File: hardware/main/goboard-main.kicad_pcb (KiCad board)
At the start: 2 copper layers, 304.7 x 135.9 mm, 152 parts, among them J1 USB_C_Receptacle_USB2.0, J2 Conn_02x05_Top_Bottom, J3 Conn_01x01, SW1 Esc, SW10 a, SW12 Fn, SW13 F2, SW14 2, SW15 w, SW16 s, SW17 z, SW18 Tux, SW19 F3, SW2 F1, SW20 3, SW21 e, SW22 d, SW23 c, SW24 Alt, SW25 F4, SW26 4, SW27 r, SW28 f, SW29 v, SW3 tilde, SW30 SW_SP3T, SW31 F5, SW32 5, SW33 t, SW34 g, SW35 b, SW36 F6, SW37 6, SW38 y, SW39 h, SW4 Tab, SW40 n, SW41 F7, SW42 7, SW43 u, SW44 j, SW45 m, SW46 Space, SW47 F8, SW48 8, SW49 i, SW5 Caps Lock, SW50 k, SW51 ,, SW52 F9, SW53 9, SW54 o, SW55 l, SW56 ., SW57 F10, SW58 0, SW59 p, SW6 Shift, SW60 ;, SW61 /, SW62 Alt Gr, SW63 F11, SW64 -, SW65 [, SW66 ', SW68 F12, SW69 =, SW7 Ctrl, SW70 ], SW71 \, SW72 Shift, SW73 Ctrl, SW74 Print, SW75 Backspace, SW76 Enter, SW77 Left, SW78 Scroll Lock, SW79 Up, SW8 1, SW80 Down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

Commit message: Change value field for the backslash-key
The value "\" caused the FreeCAD-StepUp load to fail due to a parsing
error.
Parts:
- SW71: value \ -> backslash
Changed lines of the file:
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@@
       (effects (font (size 1 1) (thickness 0.15)))
     )
-    (fp_text value "\\" (at -2.54 12.954) (layer "F.Fab")
+    (fp_text value "backslash" (at -2.54 12.954) (layer "F.Fab")
       (effects (font (size 1 1) (thickness 0.15)))
     )

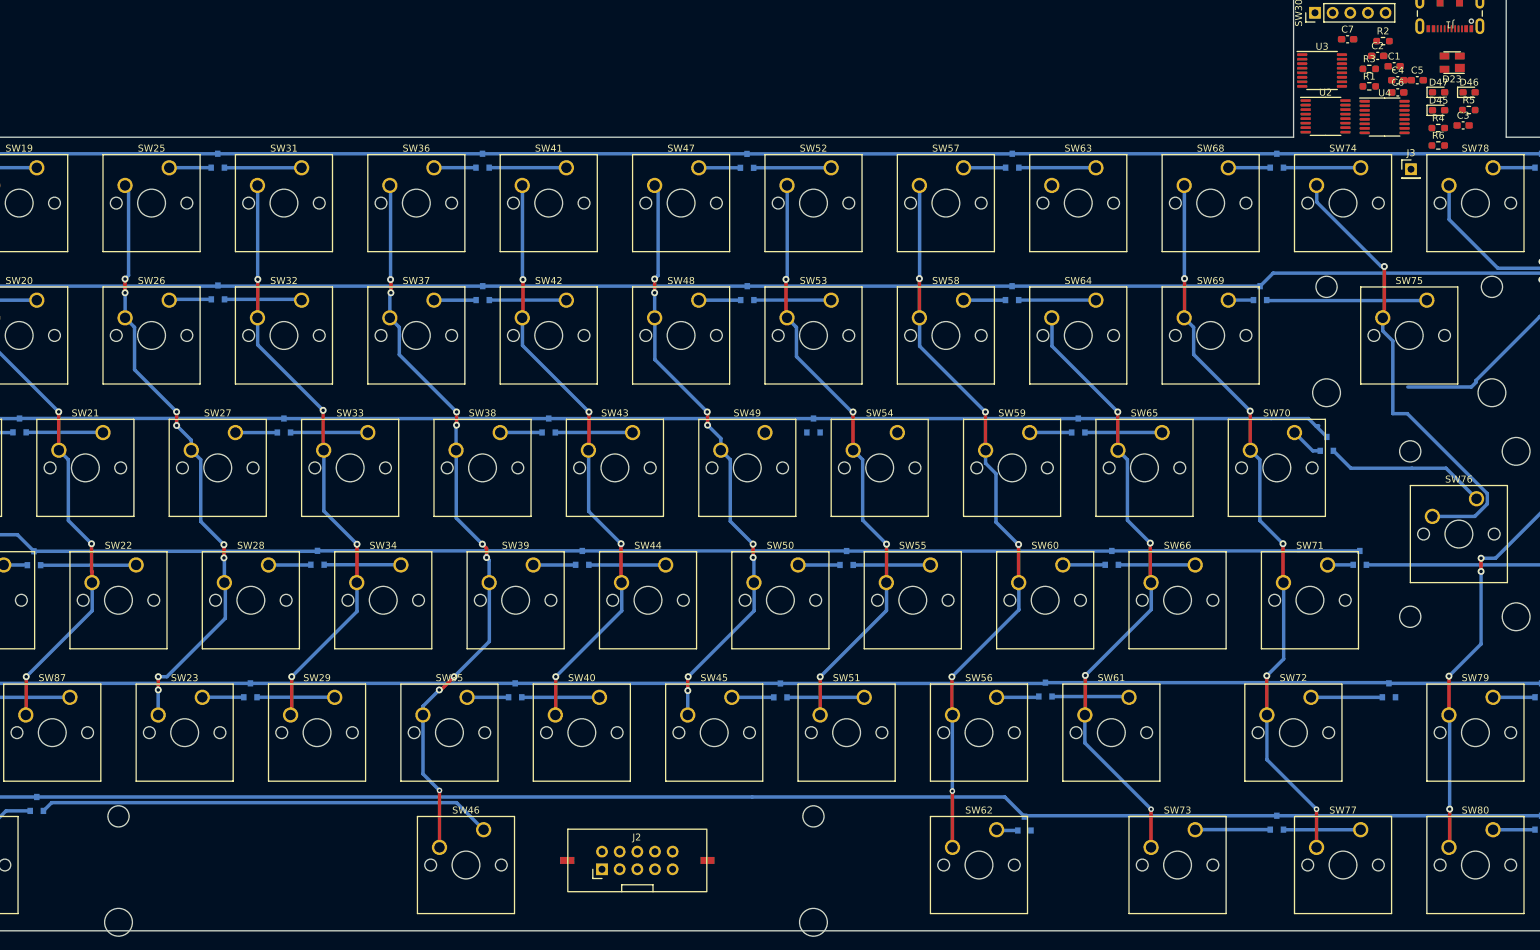
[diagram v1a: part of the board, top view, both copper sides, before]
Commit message: Write out the symbol names for the keys
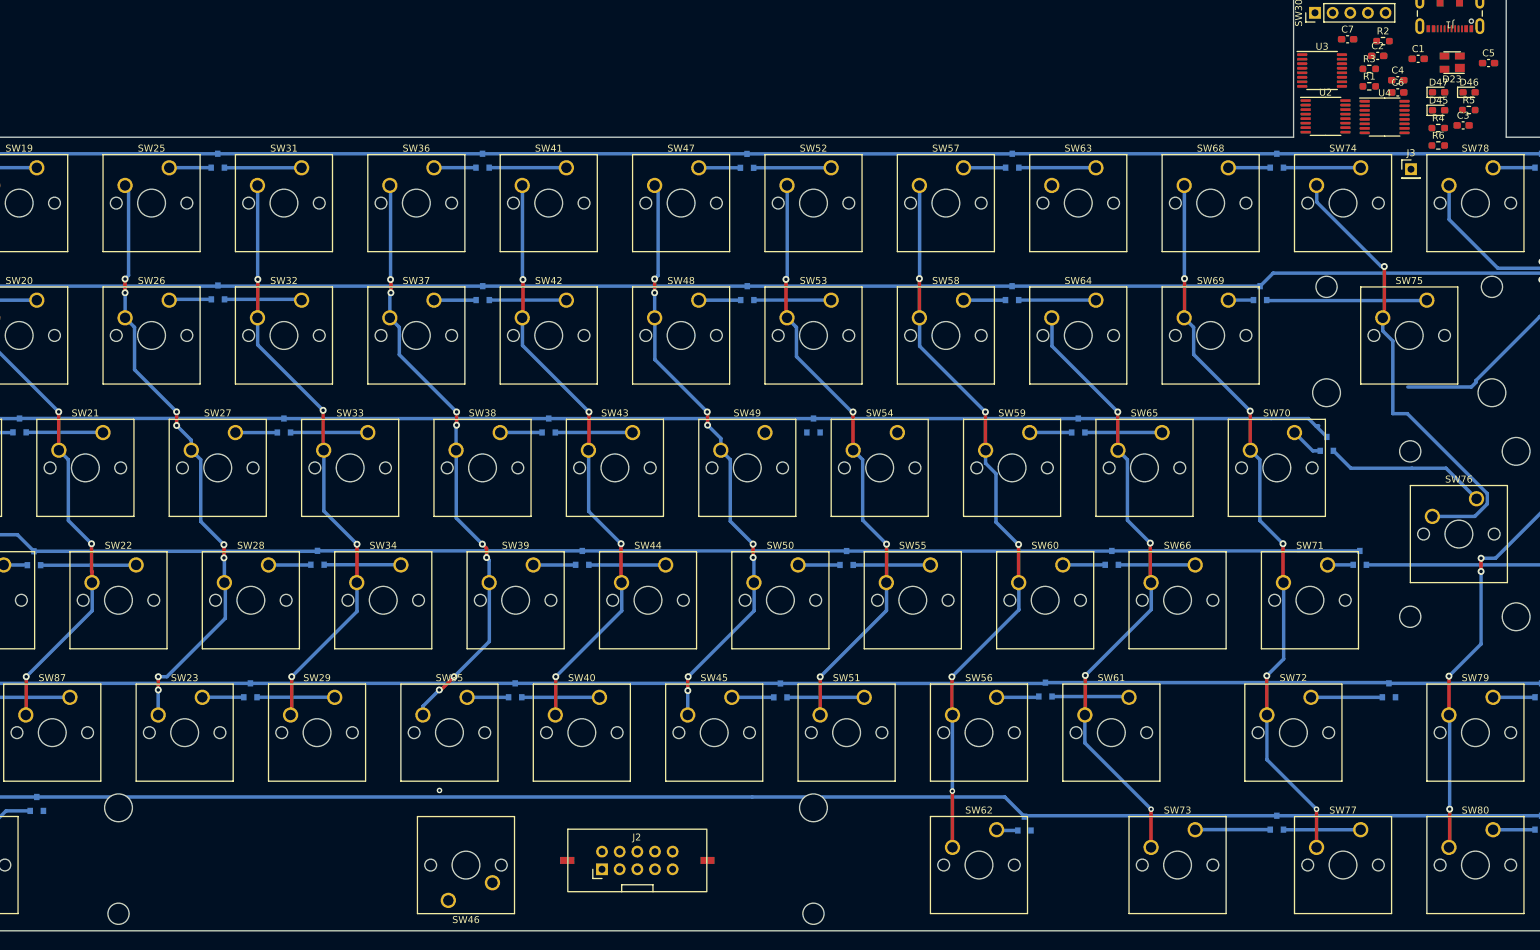
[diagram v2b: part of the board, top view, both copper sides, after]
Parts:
- SW51: value , -> comma
- SW56: value . -> dot
- SW60: value ; -> semicolon
- SW61: value / -> slash
- SW64: value - -> minus
- SW65: value [ -> sq br open
- SW66: value ' -> apostrophe
- SW69: value = -> equal
- SW70: value ] -> sq br close
- moved SW46 11.4 mm to (166.4, 181.6), turned to 180 degrees
- moved C5 10.6 mm to (316.1, 61.1)
- moved C1 3.62 mm to (305.9, 60.5)
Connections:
- net Net-(D39-Pad1) renamed no_connect_(D39-Pad1)
- net Net-(SW30-Pad1) renamed no_connect_(SW30-Pad1)
- net Net-(SW30-Pad2) renamed no_connect_(SW30-Pad2)
- net Net-(SW30-Pad3) renamed no_connect_(SW30-Pad3)
- net Net-(SW30-Pad4) renamed no_connect_(SW30-Pad4)
- net no_connect_150 renamed no_connect_(D40-Pad1)
- net no_connect_151 renamed no_connect_(J1-PadA8)
- net no_connect_152 renamed no_connect_(J1-PadB8)
- net no_connect_153 renamed no_connect_(J2-Pad10)
- net no_connect_154 renamed no_connect_(J2-Pad3)
- net no_connect_155 renamed no_connect_(J2-Pad5)
- net no_connect_156 renamed no_connect_(U1-Pad10)
- net no_connect_157 renamed no_connect_(U1-Pad11)
- net no_connect_158 renamed no_connect_(U1-Pad18)
- net no_connect_159 renamed no_connect_(U1-Pad19)
- net no_connect_160 renamed no_connect_(U1-Pad2)
- net no_connect_161 renamed no_connect_(U1-Pad26)
- net no_connect_162 renamed no_connect_(U1-Pad3)
- net no_connect_163 renamed no_connect_(U1-Pad33)
- net no_connect_164 renamed no_connect_(U1-Pad34)
- net no_connect_165 renamed no_connect_(U1-Pad35)
- net no_connect_166 renamed no_connect_(U1-Pad36)
- net no_connect_167 renamed no_connect_(U1-Pad38)
- net no_connect_168 renamed no_connect_(U1-Pad39)
- net no_connect_169 renamed no_connect_(U1-Pad4)
- net no_connect_170 renamed no_connect_(U1-Pad40)
- net no_connect_171 renamed no_connect_(U1-Pad41)
- net no_connect_172 renamed no_connect_(U1-Pad42)
- net no_connect_173 renamed no_connect_(U1-Pad43)
- net no_connect_174 renamed no_connect_(U1-Pad44)
- net no_connect_175 renamed no_connect_(U1-Pad45)
- net no_connect_176 renamed no_connect_(U1-Pad46)
- net no_connect_177 renamed no_connect_(U1-Pad47)
- net no_connect_178 renamed no_connect_(U1-Pad48)
- net no_connect_179 renamed no_connect_(U1-Pad49)
- net no_connect_180 renamed no_connect_(U1-Pad5)
- net no_connect_181 renamed no_connect_(U1-Pad50)
- net no_connect_182 renamed no_connect_(U1-Pad51)
- net no_connect_183 renamed no_connect_(U1-Pad52)
- net no_connect_184 renamed no_connect_(U1-Pad53)
- net no_connect_185 renamed no_connect_(U1-Pad54)
- net no_connect_186 renamed no_connect_(U1-Pad55)
- net no_connect_187 renamed no_connect_(U1-Pad6)
- net no_connect_188 renamed no_connect_(U1-Pad7)
- net no_connect_189 renamed no_connect_(U1-Pad8)
- net no_connect_190 renamed no_connect_(U1-Pad9)
- net no_connect_191 renamed no_connect_(U2-Pad6)
- net no_connect_192 renamed no_connect_(U2-Pad7)
- net no_connect_193 renamed no_connect_(U2-Pad9)
- net no_connect_194 renamed no_connect_(U3-Pad7)
- net no_connect_195 renamed no_connect_(U4-Pad10)
- net no_connect_196 renamed no_connect_(U4-Pad7)
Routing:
- net Net-(D12-Pad1): track 65.4 -> 0.00 mm
- net Net-(SW35-Pad2): track 106.5 -> 86.5 mm
- net Net-(D40-Pad2): track 10.8 -> 21.9 mm
- net Net-(D34-Pad1): track 11.1 -> 0.00 mm

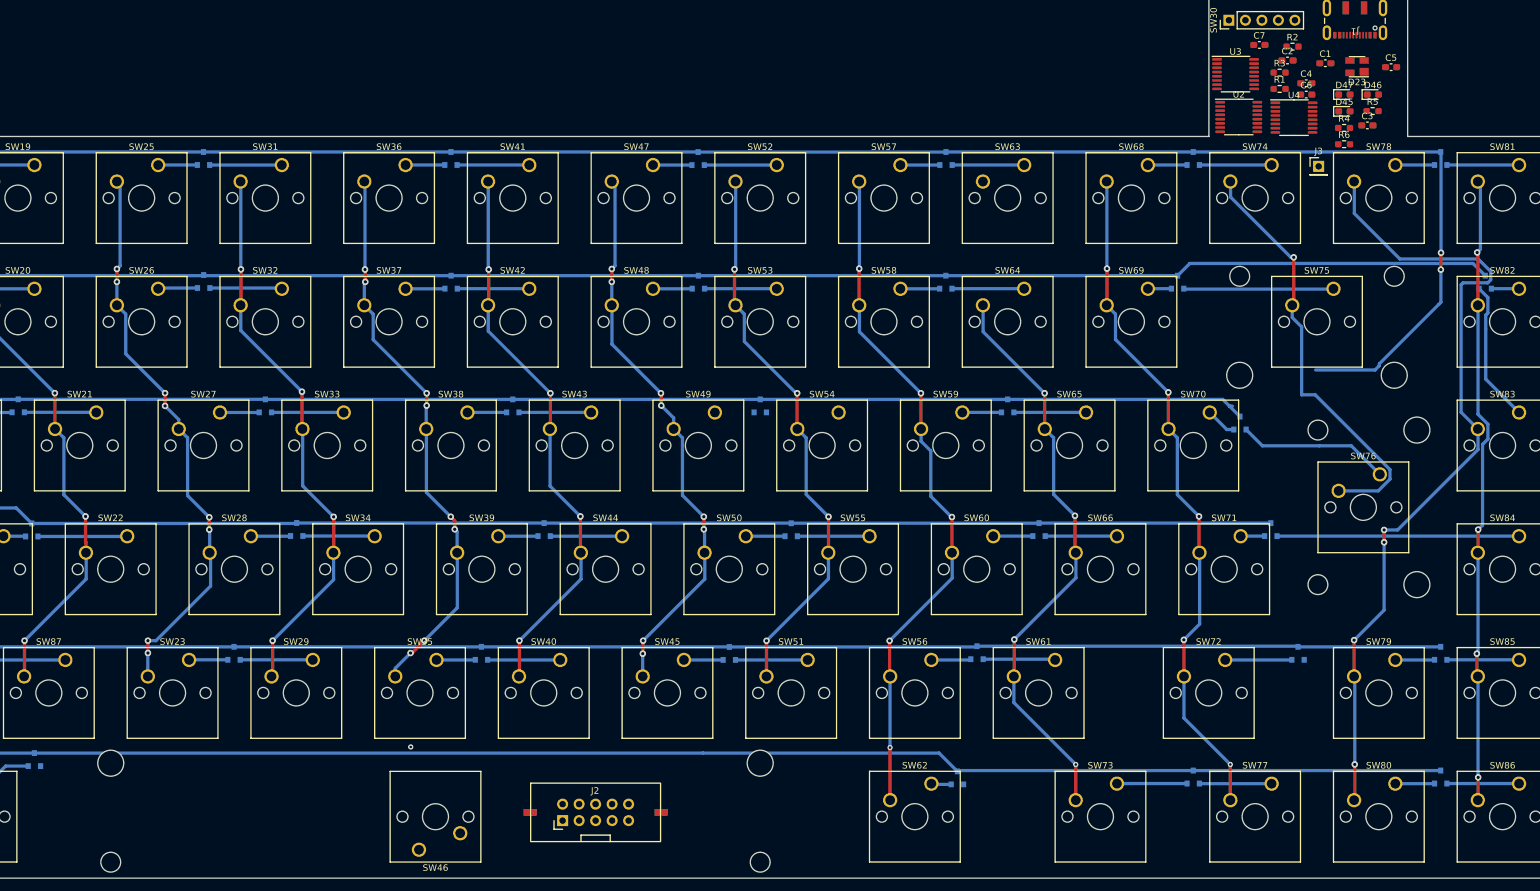
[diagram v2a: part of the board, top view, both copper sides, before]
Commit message: Revert to a key layout with a menu key between alt gr and ctrl
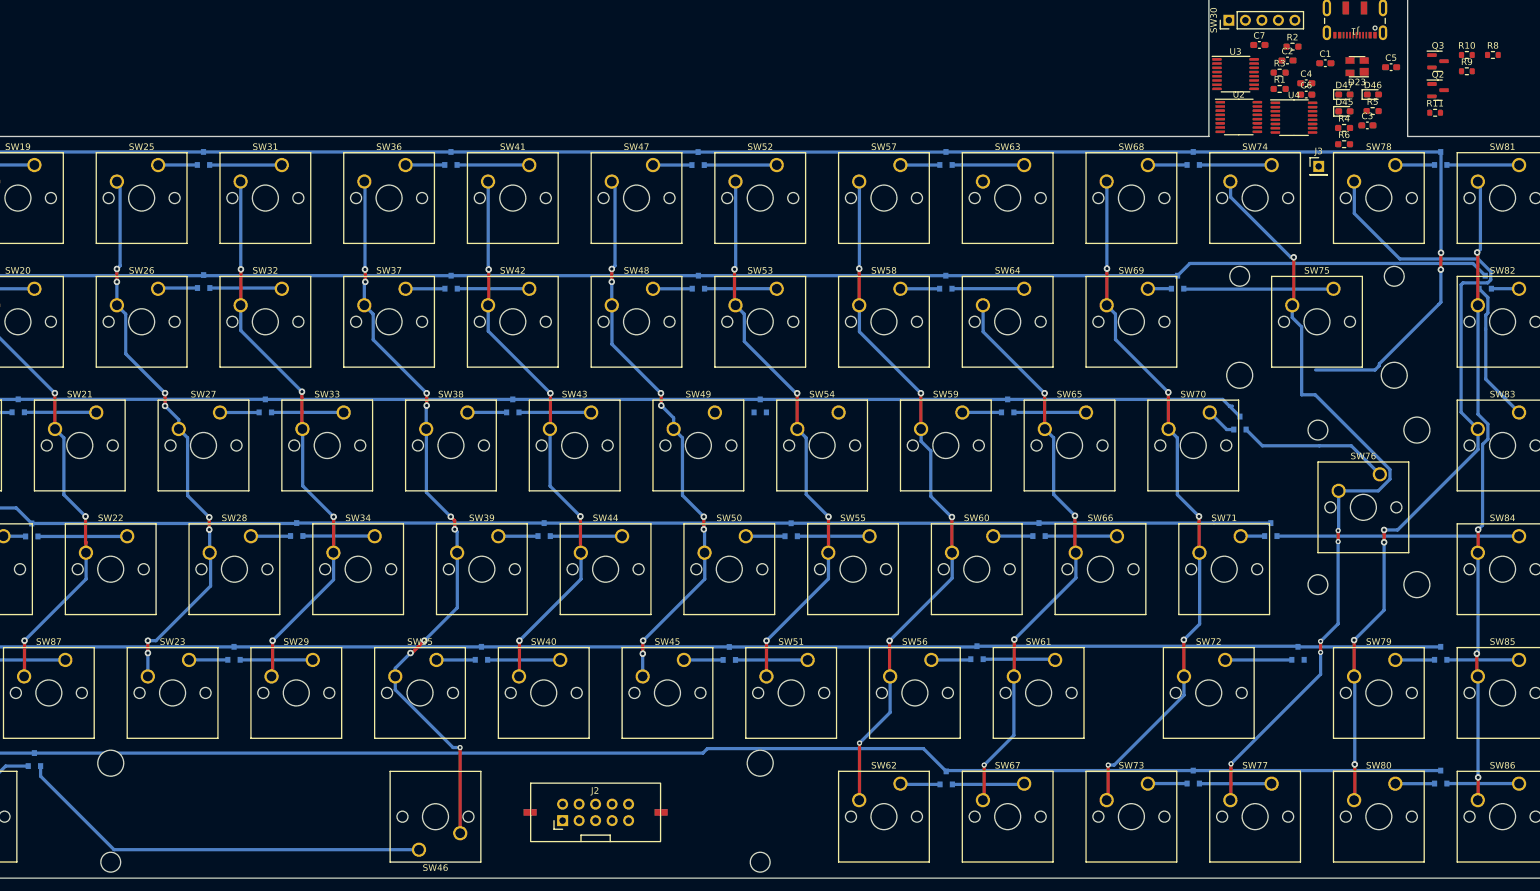
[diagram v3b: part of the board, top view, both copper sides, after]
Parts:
- added Q2: BC807, Package_TO_SOT_SMD:SOT-23, F.Cu at (323.3, 64.7)
- added Q3: BC817, Package_TO_SOT_SMD:SOT-23, F.Cu at (323.3, 60.2)
- added R10: 30, Resistor_SMD:R_0603_1608Metric, F.Cu at (327.7, 59.2)
- added R11: 30, Resistor_SMD:R_0603_1608Metric, F.Cu at (322.8, 68.2)
- added R8: 1K, Resistor_SMD:R_0603_1608Metric, F.Cu at (331.7, 59.2)
- added R9: 1K, Resistor_SMD:R_0603_1608Metric, F.Cu at (327.7, 61.8)
- added SW67: Menu, footprints:SW_Cherry_MX_1.00u_PCB, F.Cu at (259.6, 171.4)
- SW62, SW73: footprint footprints:SW_Cherry_MX_1.50u_PCB -> footprints:SW_Cherry_MX_1.00u_PCB
- moved SW62 4.76 mm to (240.5, 171.4)
- moved SW73 4.76 mm to (278.6, 171.4)
- moved D34 1.72 mm to (247.6, 170.6)
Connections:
- D40 pad 1: no_connect_(D40-Pad1) -> Net-(D40-Pad1)
- SW73 pad 1: Net-(D34-Pad1) -> Net-(D40-Pad2)
- SW73 pad 2: Net-(SW61-Pad2) -> Net-(SW68-Pad2)
- SW77 pad 1: Net-(D40-Pad2) -> Net-(D40-Pad1)
- SW77 pad 2: Net-(SW68-Pad2) -> Net-(SW74-Pad2)
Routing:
- net Net-(D12-Pad1): track 0.00 -> 64.5 mm
- net Net-(SW74-Pad2): track 66.4 -> 120.9 mm, vias 1 -> 6
- net Net-(SW35-Pad2): track 86.5 -> 115.4 mm
- net Net-(D40-Pad2): track 21.9 -> 6.04 mm
- net Net-(D40-Pad1): track 0.00 -> 11.1 mm
- net Net-(D34-Pad1): track 0.00 -> 11.1 mm
- net Net-(D34-Pad2): track 3.10 -> 6.14 mm
- net Net-(SW68-Pad2): track 105.2 -> 107.7 mm
- net Net-(SW61-Pad2): track 90.0 -> 88.1 mm
- net Net-(SW56-Pad2): track 105.4 -> 107.3 mm
- net Net-(D12-Pad3): track 267.1 -> 267.7 mm

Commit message: Add footprint and 3D-model for the sliding switch
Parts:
- added BT1: NiMH, Connector_PinHeader_2.54mm:PinHeader_1x02_P2.54mm_Horizontal, F.Cu at (145.9, 56.2)
- added BT2: NiMH, Connector_PinHeader_2.54mm:PinHeader_1x02_P2.54mm_Horizontal, F.Cu at (160.1, 56.3)
- added C10: 10uF/6.3V, Capacitor_SMD:C_0805_2012Metric, F.Cu at (203.8, 55.3)
- added C11: 10uF/6.3V, Capacitor_SMD:C_0805_2012Metric, F.Cu at (217.2, 39.9)
- added C8: 10uF/6.3V, Capacitor_SMD:C_0805_2012Metric, F.Cu at (217.2, 42.9)
- added C9: 10uF/6.3V, Capacitor_SMD:C_0805_2012Metric, F.Cu at (225.6, 35.4)
- added D48: BAT54C, Package_TO_SOT_SMD:SOT-23, F.Cu at (221.0, 36.1)
- added JP1: Battery, Connector_PinHeader_2.54mm:PinHeader_1x02_P2.54mm_Horizontal, F.Cu at (135.8, 54.6)
- added Q1: SSM3J338R, Package_TO_SOT_SMD:SOT-23_Handsoldering, F.Cu at (211.8, 43.4)
- added Q2: BCP53, Package_TO_SOT_SMD:SOT-223, F.Cu at (203.6, 45.2)
- added Q3: SSM3J338R, Package_TO_SOT_SMD:SOT-23_Handsoldering, F.Cu at (198.3, 51.6)
- added Q4: BC817, Package_TO_SOT_SMD:SOT-23, F.Cu at (211.0, 47.9)
- added Q5: SSM3J338R, Package_TO_SOT_SMD:SOT-23_Handsoldering, F.Cu at (215.3, 36.1)
- added Q8: BC817, Package_TO_SOT_SMD:SOT-23, F.Cu at (204.0, 51.5)
- added R10: 47, Resistor_SMD:R_0603_1608Metric, F.Cu at (215.4, 46.9)
- added R11: 1K, Resistor_SMD:R_0603_1608Metric, F.Cu at (221.4, 39.6)
- added R12: 0.5, Resistor_SMD:R_1206_3216Metric, F.Cu at (197.9, 55.5)
- added R13: 1K, Resistor_SMD:R_0603_1608Metric, F.Cu at (225.4, 38.1)
- added R14: 10K, Resistor_SMD:R_0603_1608Metric, F.Cu at (212.5, 51.3)
- added R19: 4.7K, Resistor_SMD:R_0603_1608Metric, F.Cu at (219.4, 45.7)
- added R20: 10K, Resistor_SMD:R_0603_1608Metric, F.Cu at (221.4, 42.1)
- added R7: 10K, Resistor_SMD:R_0603_1608Metric, F.Cu at (208.0, 55.0)
- added R8: 100K, Resistor_SMD:R_0603_1608Metric, F.Cu at (225.4, 40.6)
- added R9: 100K, Resistor_SMD:R_0603_1608Metric, F.Cu at (208.5, 51.3)
- added U5: AP2114H-3.3, Package_TO_SOT_SMD:SOT-223-3_TabPin2, F.Cu at (138.0, 66.9)
- SW30: value SW_SP3T -> SW_DP3T; footprint Connector_PinHeader_2.54mm:PinHeader_1x05_P2.54mm_Vertical -> footprints:EG2315A
- moved U1 210.1 mm to (269.7, 53.5)
- moved SW30 13.1 mm to (298.0, 42.8), turned to 180 degrees
- moved R2 2.79 mm to (303.5, 58.9)
- moved C7 2.22 mm to (297.7, 58.8)
- renumbered Q2 to Q6, Q3 to Q7, R8 to R15, R9 to R16, R10 to R17, R11 to R18
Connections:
- C3 pad 1: /MCU/VCC_SW -> /VCC_SW
- C4 pad 1: /keys/VCC_SW -> /VCC_SW
- D39 pad 1: no_connect_(D39-Pad1) -> unconnected-(D39-Pad1)
- J1 pad A8: no_connect_(J1-PadA8) -> unconnected-(J1-PadA8)
- J1 pad B8: no_connect_(J1-PadB8) -> unconnected-(J1-PadB8)
- J2 pad 10: no_connect_(J2-Pad10) -> unconnected-(J2-Pad10)
- J2 pad 3: no_connect_(J2-Pad3) -> unconnected-(J2-Pad3)
- J2 pad 5: no_connect_(J2-Pad5) -> unconnected-(J2-Pad5)
- SW30 pad 1: no_connect_(SW30-Pad1) -> /switch_usb_off
- SW30 pad 2: no_connect_(SW30-Pad2) -> /switch_bt_1
- SW30 pad 3: no_connect_(SW30-Pad3) -> /VCC_SW
- SW30 pad 4: no_connect_(SW30-Pad4) -> /switch_bt_2
- U1 pad 10: no_connect_(U1-Pad10) -> unconnected-(U1-Pad10)
- U1 pad 11: no_connect_(U1-Pad11) -> unconnected-(U1-Pad11)
- U1 pad 14: /MCU/VCC_SW -> /VCC_SW
- U1 pad 18: no_connect_(U1-Pad18) -> unconnected-(U1-Pad18)
- U1 pad 19: no_connect_(U1-Pad19) -> unconnected-(U1-Pad19)
- U1 pad 2: no_connect_(U1-Pad2) -> unconnected-(U1-Pad2)
- U1 pad 26: no_connect_(U1-Pad26) -> unconnected-(U1-Pad26)
- U1 pad 3: no_connect_(U1-Pad3) -> /switch_bt_2
- U1 pad 33: no_connect_(U1-Pad33) -> /switch_usb_off
- U1 pad 34: no_connect_(U1-Pad34) -> /switch_bt_1
- U1 pad 35: no_connect_(U1-Pad35) -> unconnected-(U1-Pad35)
- U1 pad 36: no_connect_(U1-Pad36) -> unconnected-(U1-Pad36)
- U1 pad 38: no_connect_(U1-Pad38) -> unconnected-(U1-Pad38)
- U1 pad 39: no_connect_(U1-Pad39) -> unconnected-(U1-Pad39)
- U1 pad 4: no_connect_(U1-Pad4) -> unconnected-(U1-Pad4)
- U1 pad 40: no_connect_(U1-Pad40) -> unconnected-(U1-Pad40)
- U1 pad 41: no_connect_(U1-Pad41) -> unconnected-(U1-Pad41)
- U1 pad 42: no_connect_(U1-Pad42) -> unconnected-(U1-Pad42)
- U1 pad 43: no_connect_(U1-Pad43) -> unconnected-(U1-Pad43)
- U1 pad 44: no_connect_(U1-Pad44) -> unconnected-(U1-Pad44)
- U1 pad 45: no_connect_(U1-Pad45) -> unconnected-(U1-Pad45)
- U1 pad 46: no_connect_(U1-Pad46) -> unconnected-(U1-Pad46)
- U1 pad 47: no_connect_(U1-Pad47) -> unconnected-(U1-Pad47)
- U1 pad 48: no_connect_(U1-Pad48) -> unconnected-(U1-Pad48)
- U1 pad 49: no_connect_(U1-Pad49) -> unconnected-(U1-Pad49)
- U1 pad 5: no_connect_(U1-Pad5) -> unconnected-(U1-Pad5)
- U1 pad 50: no_connect_(U1-Pad50) -> unconnected-(U1-Pad50)
- U1 pad 51: no_connect_(U1-Pad51) -> unconnected-(U1-Pad51)
- U1 pad 52: no_connect_(U1-Pad52) -> unconnected-(U1-Pad52)
- U1 pad 53: no_connect_(U1-Pad53) -> unconnected-(U1-Pad53)
- U1 pad 54: no_connect_(U1-Pad54) -> unconnected-(U1-Pad54)
- U1 pad 55: no_connect_(U1-Pad55) -> unconnected-(U1-Pad55)
- U1 pad 6: no_connect_(U1-Pad6) -> unconnected-(U1-Pad6)
- U1 pad 7: no_connect_(U1-Pad7) -> unconnected-(U1-Pad7)
- U1 pad 8: no_connect_(U1-Pad8) -> unconnected-(U1-Pad8)
- U1 pad 9: no_connect_(U1-Pad9) -> unconnected-(U1-Pad9)
- U2 pad 10: /keys/VCC_SW -> /VCC_SW
- U2 pad 6: no_connect_(U2-Pad6) -> unconnected-(U2-Pad6)
- U2 pad 7: no_connect_(U2-Pad7) -> unconnected-(U2-Pad7)
- U2 pad 9: no_connect_(U2-Pad9) -> unconnected-(U2-Pad9)
- U3 pad 16: /keys/VCC_SW -> /VCC_SW
- U3 pad 7: no_connect_(U3-Pad7) -> unconnected-(U3-Pad7)
- U4 pad 10: no_connect_(U4-Pad10) -> unconnected-(U4-Pad10)
- U4 pad 16: /keys/VCC_SW -> /VCC_SW
- U4 pad 7: no_connect_(U4-Pad7) -> unconnected-(U4-Pad7)
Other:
- outline, holes or cut-outs redrawn
